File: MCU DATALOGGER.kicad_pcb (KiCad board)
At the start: 2 copper layers, 54.3 x 31.6 mm, 29 parts, among them J1 Conn_01x04_Pin, J2 Conn_01x04_Pin, J3 Conn_01x09_Pin, J4 Conn_02x03_Odd_Even, U1 24LC1025, U2 DS1337S_, U3 24LC1025, U4 ATMEGA328P-AU, Y1 32.768 KHz, Y2 16 MHz

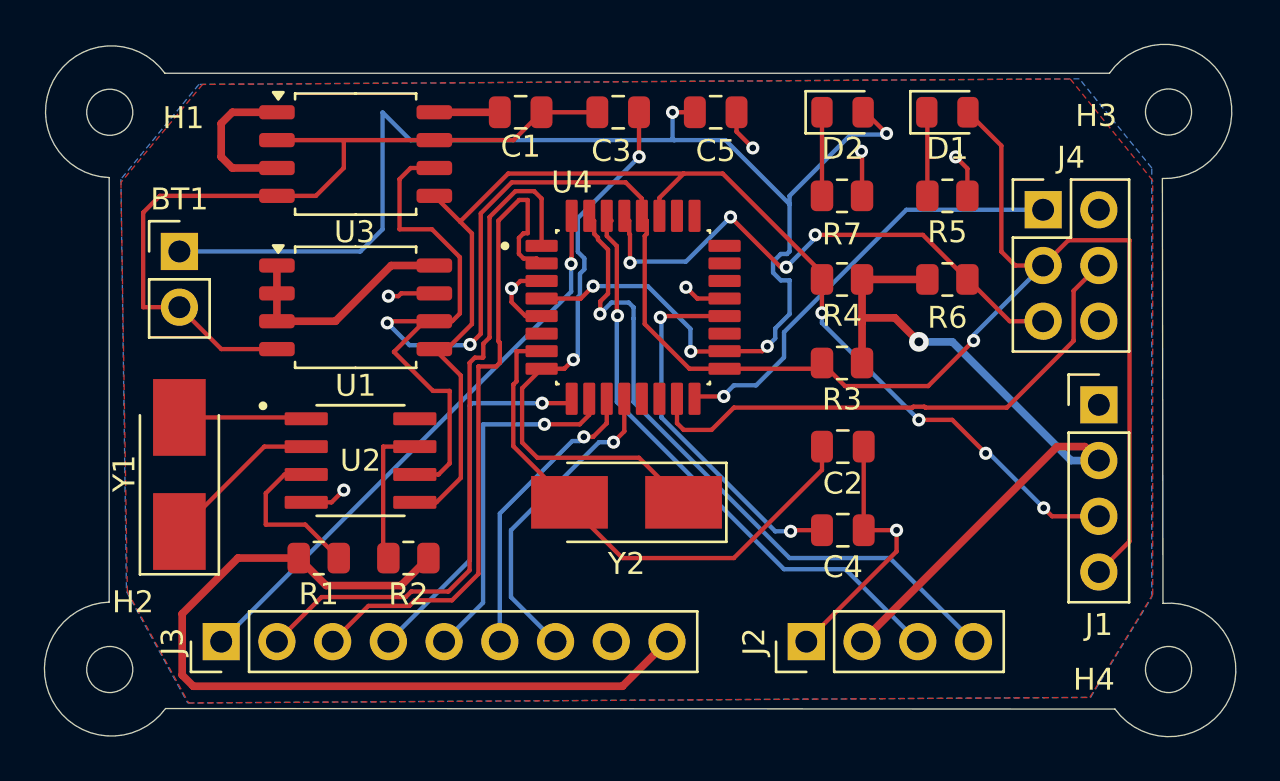
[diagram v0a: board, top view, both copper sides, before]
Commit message: Updated PCB For 2 Layer
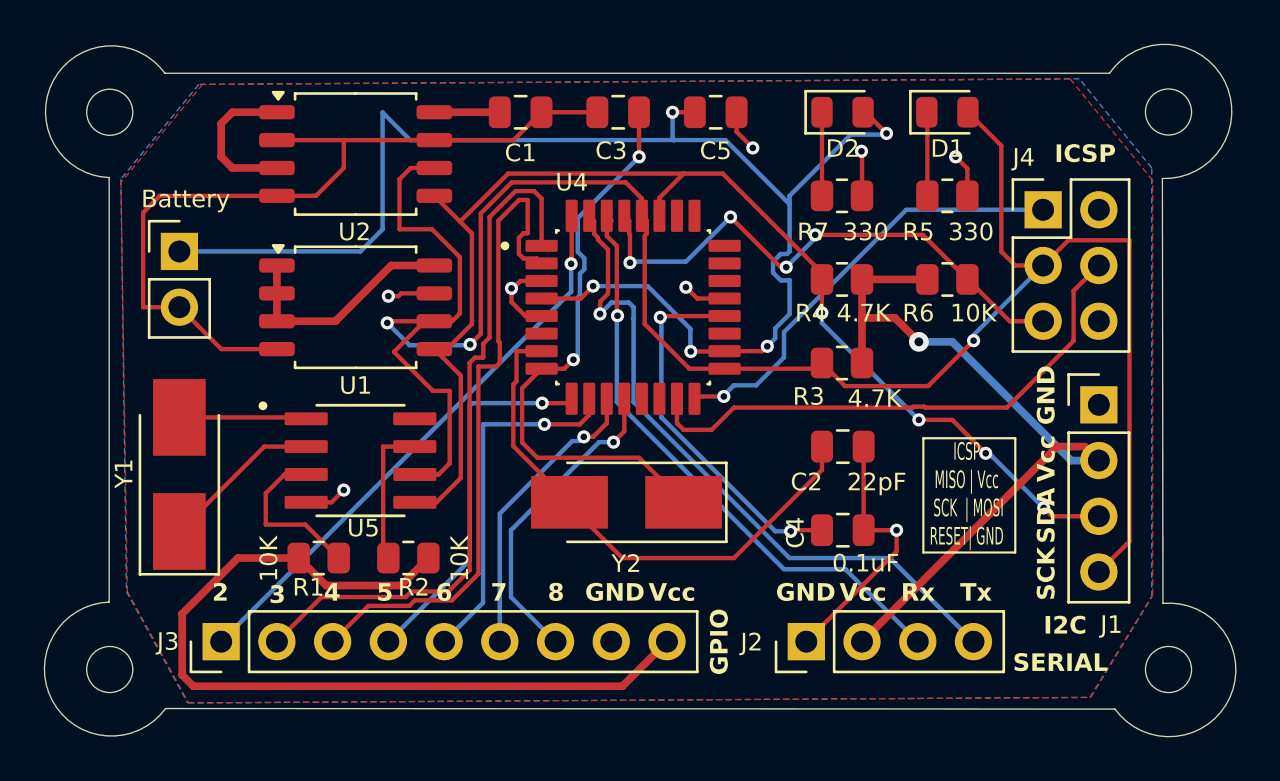
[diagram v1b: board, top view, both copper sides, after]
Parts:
- renumbered U3 to U2, U2 to U5
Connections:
- BT1 pad 1: Net-(BT1-+) -> /Vcc
- C5 pad 1: Net-(BT1-+) -> /Vcc
- D2 pad 2: Net-(BT1-+) -> /Vcc
- U4 pad 18: Net-(BT1-+) -> /Vcc
- U4 pad 4: Net-(BT1-+) -> /Vcc
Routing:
- net Net-(BT1-+): track 65.4 -> 0.00 mm, vias 5 -> 0
- net /Vcc: track 95.2 -> 160.6 mm, vias 1 -> 6
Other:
- board text added: "2"
- board text added: "3"
- board text added: "4"
- board text added: "5"
- board text added: "6"
- board text added: "7"
- board text added: "8"
- board text added: "GND"
- board text added: "GPIO"
- board text added: "I2C"
- board text added: "ICSP"
- board text added: "ICSP MISO | Vcc SCK | MOSI RESET| GND"
- board text added: "Rx"
- board text added: "SCK"
- board text added: "SDA"
- board text added: "SERIAL"
- board text added: "Tx"
- board text added: "Vcc"

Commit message: Updated
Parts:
- added REF**: KiCad-Logo2_5mm_SilkScreen, Symbol:KiCad-Logo2_5mm_SilkScreen, B.Cu at (102.9, 61.0)

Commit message: Updated
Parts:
- moved REF** 13.7 mm to (90.2, 55.9)
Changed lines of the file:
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@@
 			(plot_on_all_layers_selection 0x00000000_00000000_00000000_00000000)
 			(disableapertmacros no)
-			(usegerberextensions no)
+			(usegerberextensions yes)
 			(usegerberattributes yes)
 			(usegerberadvancedattributes yes)
@@
 			(outputformat 1)
 			(mirror no)
-			(drillshape 1)
+			(drillshape 0)
 			(scaleselection 1)
-			(outputdirectory "")
+			(outputdirectory "GERBER/")
 		)
 	)
@@
 	(footprint "Symbol:KiCad-Logo2_5mm_SilkScreen"
 		(layer "B.Cu")
-		(at 102.87 60.96 180)
+		(at 90.17 55.88 180)
 		(descr "KiCad Logo")
 		(tags "Logo KiCad")
@@
 	)
 	(gr_line
-		(start 115.824 73.406)
-		(end 120.0023 73.406)
+		(start 115.4 70.0035)
+		(end 119.5783 70.0035)
 		(stroke
 			(width 0.1)
@@
 	)
 	(gr_line
-		(start 120.015 73.406)
-		(end 120.015 68.199)
+		(start 119.591 70.0035)
+		(end 119.591 64.7965)
 		(stroke
 			(width 0.1)
@@
 	)
 	(gr_line
-		(start 120.015 68.199)
-		(end 115.824 68.199)
+		(start 119.591 64.7965)
+		(end 115.4 64.7965)
 		(stroke
 			(width 0.1)
@@
 	)
 	(gr_line
-		(start 115.824 68.199)
-		(end 115.824 73.406)
+		(start 115.4 64.7965)
+		(end 115.4 70.0035)
 		(stroke
 			(width 0.1)
@@
 	)
 	(gr_text "ICSP\nMISO | Vcc\n SCK  | MOSI\nRESET| GND"
-		(at 117.8 73.14 0)
+		(at 117.376 69.7375 0)
 		(layer "F.SilkS")
 		(effects

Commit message: Updated
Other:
- board text added: "0.2000 mm / 0.0000 mm"
- board text added: "0.3000 mm"
- board text added: "1.6000 mm"
- board text added: "54.3109 mm x 31.5621 mm"
- board text added: "BOARD CHARACTERISTICS"
- board text added: "Board Thickness:"
- board text added: "Board overall dimensions:"
- board text added: "Castellated pads:"
- board text added: "Copper Finish:"
- board text added: "Copper Layer Count:"
- board text added: "Edge card connectors:"
- board text added: "Impedance Control:"
- board text added: "Min hole diameter:"
- board text added: "Min track/spacing:"
- board text added: "No"
- board text added: "None"
- board text added: "Plated Board Edge:"
